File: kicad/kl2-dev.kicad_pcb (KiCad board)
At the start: 2 copper layers, 34.3 x 19 mm, 16 parts, among them CON1 USB-MINI-B, P1 CONN_13, P2 CONN_13, P3 TST, U1 MKL26Z32VFM4, X1 CRYSTAL

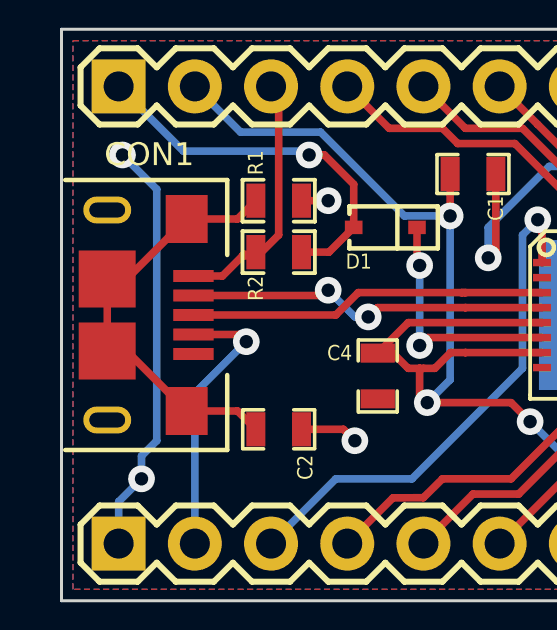
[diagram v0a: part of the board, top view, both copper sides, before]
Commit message: Fixed oval holes to be large circles
OSHPark didn't handle them very well
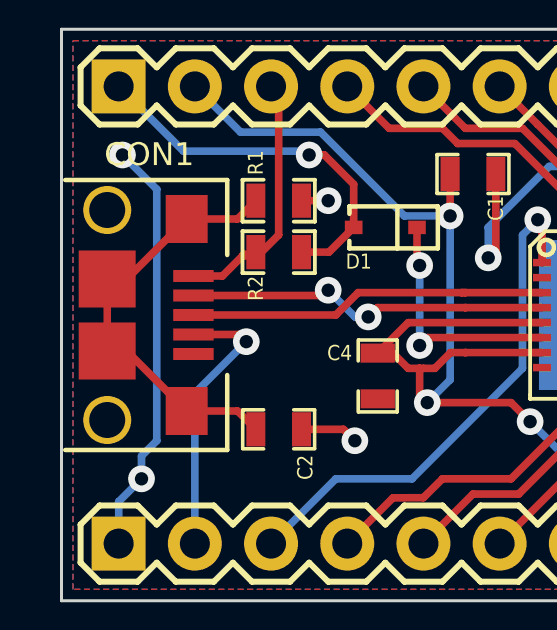
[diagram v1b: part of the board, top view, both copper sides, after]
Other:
- board text added: "kl2-dev"
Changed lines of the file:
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@@
     (links 58)
     (no_connects 1)
-    (area 33.349767 46.7335 69.265001 69.4674)
+    (area 33.349767 47.3726 69.265001 69.4674)
     (thickness 1.6)
-    (drawings 7)
+    (drawings 6)
     (tracks 261)
     (zones 0)
@@
     (mod_text_size 1 1)
     (mod_text_width 0.15)
-    (pad_size 5 5)
-    (pad_drill 0)
+    (pad_size 1.6 1.6)
+    (pad_drill 1.2)
     (pad_to_mask_clearance 0)
     (aux_axis_origin 0 0)
@@
     )
   )
-  (module USB-MICRO-B (layer F.Cu)
-    (at 36.449 58.42 270)
-    (fp_text reference CON1 (at -5.35 -1.4 360) (layer F.SilkS)
-      (effects (font (size 0.762 0.762) (thickness 0.127)))
-    )
-    (fp_text value USB-MINI-B (at 5.4 -1.35 360) (layer F.SilkS) hide
-      (effects (font (size 0.762 0.762) (thickness 0.127)))
-    )
-    (fp_line (start 4.5 1.4) (end 4.5 -4) (layer F.SilkS) (width 0.15))
-    (fp_line (start 4.5 -4) (end 2 -4) (layer F.SilkS) (width 0.15))
-    (fp_line (start -4.5 1.4) (end -4.5 -4) (layer F.SilkS) (width 0.15))
-    (fp_line (start -4.5 -4) (end -2 -4) (layer F.SilkS) (width 0.15))
-    (pad 6 smd rect (at -1.2 0 270) (size 1.9 1.9)
-      (layers F.Cu F.Paste F.Mask)
-      (net 28 N-0000013)
-    )
-    (pad 7 smd rect (at 1.2 0 270) (size 1.9 1.9)
-      (layers F.Cu F.Paste F.Mask)
-      (net 28 N-0000013)
-    )
-    (pad 8 smd rect (at -3.2 -2.65 270) (size 1.6 1.4)
-      (layers F.Cu F.Paste F.Mask)
-      (net 28 N-0000013)
-    )
-    (pad 9 smd rect (at 3.2 -2.65 270) (size 1.6 1.4)
-      (layers F.Cu F.Paste F.Mask)
-      (net 28 N-0000013)
-    )
-    (pad 3 smd rect (at 0 -2.875 270) (size 0.4 1.35)
-      (layers F.Cu F.Paste F.Mask)
-      (net 26 N-0000011)
-    )
-    (pad 4 smd rect (at 0.65 -2.875 270) (size 0.4 1.35)
-      (layers F.Cu F.Paste F.Mask)
-      (net 2 /ID)
-    )
-    (pad 2 smd rect (at -0.65 -2.875 270) (size 0.4 1.35)
-      (layers F.Cu F.Paste F.Mask)
-      (net 27 N-0000012)
-    )
-    (pad 1 smd rect (at -1.3 -2.875 270) (size 0.4 1.35)
-      (layers F.Cu F.Paste F.Mask)
-      (net 31 N-0000025)
-    )
-    (pad 5 smd rect (at 1.3 -2.875 270) (size 0.4 1.35)
-      (layers F.Cu F.Paste F.Mask)
-      (net 25 GND)
-    )
-    (pad 10 thru_hole oval (at -3.5 0 270) (size 0.9 1.6) (drill oval 0.5 1.2)
-      (layers *.Cu *.Mask F.SilkS)
-    )
-    (pad 11 thru_hole oval (at 3.5 0 270) (size 0.9 1.6) (drill oval 0.5 1.2)
-      (layers *.Cu *.Mask F.SilkS)
-    )
-  )
   (module SOD323 (layer F.Cu)
     (at 45.72 55.499)
@@
     )
   )
+  (module USB-MICRO-B (layer F.Cu)
+    (at 36.449 58.42 270)
+    (fp_text reference CON1 (at -5.35 -1.4 360) (layer F.SilkS)
+      (effects (font (size 0.762 0.762) (thickness 0.127)))
+    )
+    (fp_text value USB-MINI-B (at 5.4 -1.35 360) (layer F.SilkS) hide
+      (effects (font (size 0.762 0.762) (thickness 0.127)))
+    )
+    (fp_line (start 4.5 1.4) (end 4.5 -4) (layer F.SilkS) (width 0.15))
+    (fp_line (start 4.5 -4) (end 2 -4) (layer F.SilkS) (width 0.15))
+    (fp_line (start -4.5 1.4) (end -4.5 -4) (layer F.SilkS) (width 0.15))
+    (fp_line (start -4.5 -4) (end -2 -4) (layer F.SilkS) (width 0.15))
+    (pad 6 smd rect (at -1.2 0 270) (size 1.9 1.9)
+      (layers F.Cu F.Paste F.Mask)
+      (net 28 N-0000013)
+    )
+    (pad 7 smd rect (at 1.2 0 270) (size 1.9 1.9)
+      (layers F.Cu F.Paste F.Mask)
+      (net 28 N-0000013)
+    )
+    (pad 8 smd rect (at -3.2 -2.65 270) (size 1.6 1.4)
+      (layers F.Cu F.Paste F.Mask)
+      (net 28 N-0000013)
+    )
+    (pad 9 smd rect (at 3.2 -2.65 270) (size 1.6 1.4)
+      (layers F.Cu F.Paste F.Mask)
+      (net 28 N-0000013)
+    )
+    (pad 3 smd rect (at 0 -2.875 270) (size 0.4 1.35)
+      (layers F.Cu F.Paste F.Mask)
+      (net 26 N-0000011)
+    )
+    (pad 4 smd rect (at 0.65 -2.875 270) (size 0.4 1.35)
+      (layers F.Cu F.Paste F.Mask)
+      (net 2 /ID)
+    )
+    (pad 2 smd rect (at -0.65 -2.875 270) (size 0.4 1.35)
+      (layers F.Cu F.Paste F.Mask)
+      (net 27 N-0000012)
+    )
+    (pad 1 smd rect (at -1.3 -2.875 270) (size 0.4 1.35)
+      (layers F.Cu F.Paste F.Mask)
+      (net 31 N-0000025)
+    )
+    (pad 5 smd rect (at 1.3 -2.875 270) (size 0.4 1.35)
+      (layers F.Cu F.Paste F.Mask)
+      (net 25 GND)
+    )
+    (pad 10 thru_hole circle (at -3.5 0 270) (size 1.6 1.6) (drill 1.2)
+      (layers *.Cu *.Mask F.SilkS)
+    )
+    (pad 11 thru_hole circle (at 3.5 0 270) (size 1.6 1.6) (drill 1.2)
+      (layers *.Cu *.Mask F.SilkS)
+    )
+  )
+  (gr_text kl2-dev (at 39.37 58.42 270) (layer B.SilkS)
+    (effects (font (size 1.5 1.5) (thickness 0.3)) (justify mirror))
+  )
   (gr_line (start 34.925 67.945) (end 34.925 48.895) (angle 90) (layer Edge.Cuts) (width 0.1))
   (gr_line (start 69.215 67.945) (end 34.925 67.945) (angle 90) (layer Edge.Cuts) (width 0.1))
   (gr_line (start 69.215 48.895) (end 69.215 67.945) (angle 90) (layer Edge.Cuts) (width 0.1))
   (gr_line (start 34.925 48.895) (end 69.215 48.895) (angle 90) (layer Edge.Cuts) (width 0.1))
-  (target plus (at 39.624 46.736) (size 0.005) (width 0.1) (layer Edge.Cuts))
-  (target plus (at 39.624 46.736) (size 0.005) (width 0.1) (layer Edge.Cuts))
   (target plus (at 36.83 50.8) (size 0.005) (width 0.1) (layer Edge.Cuts))
   (segment (start 47.117 61.341) (end 49.911 61.341) (width 0.254) (layer F.Cu) (net 1))

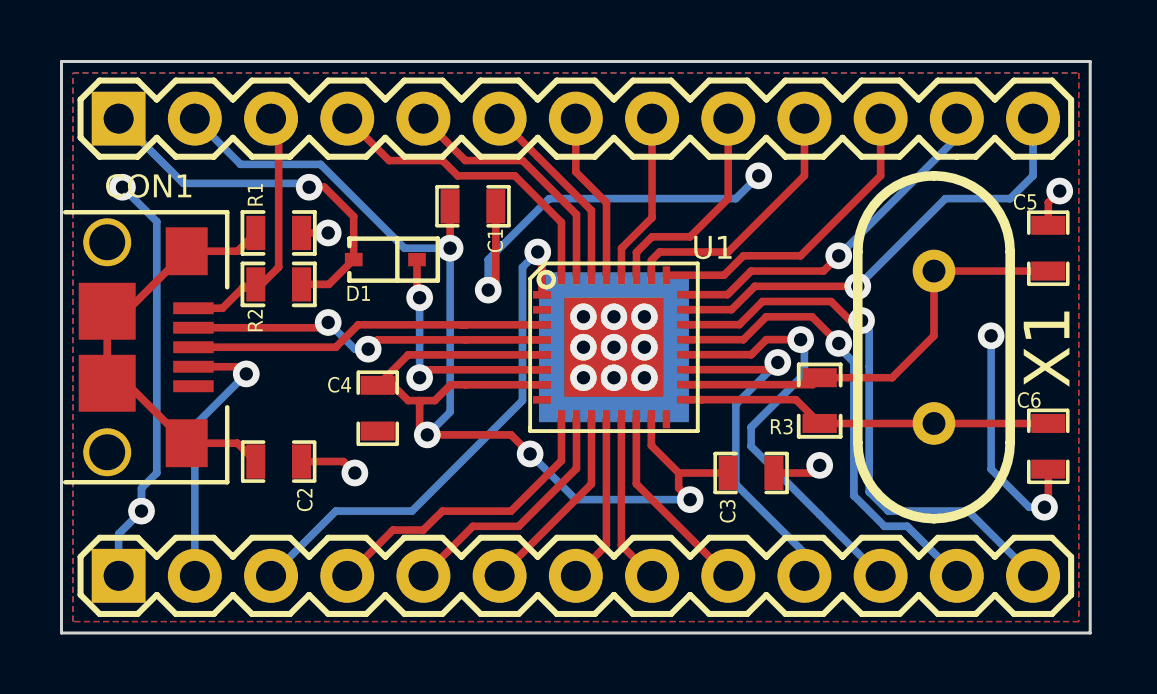
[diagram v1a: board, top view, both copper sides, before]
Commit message: Reduced thermal via size to minimum drill diameter
TI has a paper about this and said to keep the via size <0.3mm (we can't quite
get that small, but we can get close) and to have the spacing of thermal vias
be about 1mm (we had this already by happenstance)
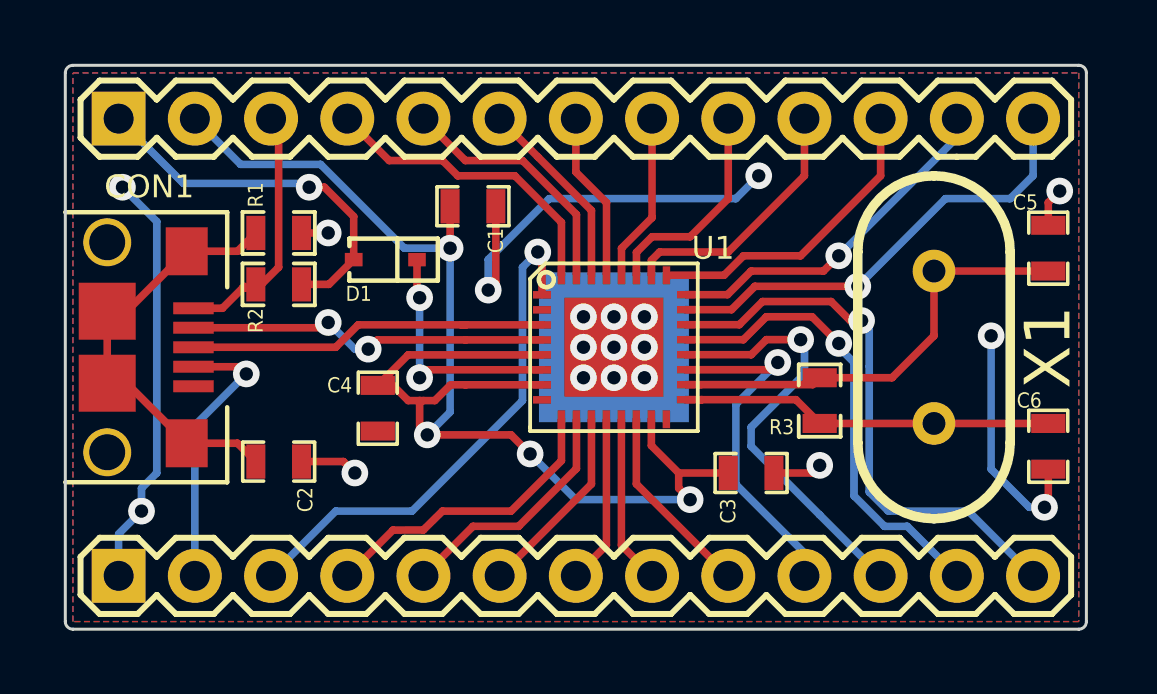
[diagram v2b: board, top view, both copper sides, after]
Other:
- board size 34.3 x 19 mm -> 34 x 18.8 mm
- net class Thermal added: clearance 0.1524, trace_width 0.254, via_dia 0.5588, via_drill 0.3302
- rule via_min_drill: 0.508 -> 0.3302
- rule via_min_size: 0.889 -> 0.508
- board text added: "KL2x ARM Dev Board Kevin Cuzner"
- board text removed: "kl2-dev"
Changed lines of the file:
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@@
     (links 58)
     (no_connects 1)
-    (area 33.349767 47.3726 69.265001 69.4674)
+    (area 33.270372 47.3726 69.138001 69.4674)
     (thickness 1.6)
-    (drawings 6)
+    (drawings 10)
     (tracks 261)
     (zones 0)
@@
     (via_size 0.889)
     (via_drill 0.635)
-    (via_min_size 0.889)
-    (via_min_drill 0.508)
+    (via_min_size 0.508)
+    (via_min_drill 0.3302)
     (uvia_size 0.508)
     (uvia_drill 0.127)
@@
     (add_net /PTE0)
     (add_net /PTE30)
-    (add_net /U1_THERM)
     (add_net GND)
     (add_net N-0000011)
@@
     (add_net N-000003)
     (add_net VDD)
+  )
+  (net_class Thermal ""
+    (clearance 0.1524)
+    (trace_width 0.254)
+    (via_dia 0.5588)
+    (via_drill 0.3302)
+    (uvia_dia 0.508)
+    (uvia_drill 0.127)
+    (add_net /U1_THERM)
   )
   (module SM0603_Resistor (layer F.Cu)
@@
     )
   )
-  (gr_text kl2-dev (at 39.37 58.42 270) (layer B.SilkS)
-    (effects (font (size 1.5 1.5) (thickness 0.3)) (justify mirror))
-  )
-  (gr_line (start 34.925 67.945) (end 34.925 48.895) (angle 90) (layer Edge.Cuts) (width 0.1))
-  (gr_line (start 69.215 67.945) (end 34.925 67.945) (angle 90) (layer Edge.Cuts) (width 0.1))
-  (gr_line (start 69.215 48.895) (end 69.215 67.945) (angle 90) (layer Edge.Cuts) (width 0.1))
-  (gr_line (start 34.925 48.895) (end 69.215 48.895) (angle 90) (layer Edge.Cuts) (width 0.1))
+  (gr_line (start 68.834 67.818) (end 35.306 67.818) (angle 90) (layer Edge.Cuts) (width 0.1))
+  (gr_line (start 69.088 49.276) (end 69.088 67.564) (angle 90) (layer Edge.Cuts) (width 0.1))
+  (gr_line (start 35.306 49.022) (end 68.834 49.022) (angle 90) (layer Edge.Cuts) (width 0.1))
+  (gr_line (start 35.052 67.564) (end 35.052 49.276) (angle 90) (layer Edge.Cuts) (width 0.1))
+  (gr_arc (start 35.306 67.564) (end 35.306 67.818) (angle 90) (layer Edge.Cuts) (width 0.1))
+  (gr_arc (start 68.834 67.564) (end 69.088 67.564) (angle 90) (layer Edge.Cuts) (width 0.1))
+  (gr_arc (start 68.834 49.276) (end 68.834 49.022) (angle 90) (layer Edge.Cuts) (width 0.1))
+  (gr_arc (start 35.306 49.276) (end 35.052 49.276) (angle 90) (layer Edge.Cuts) (width 0.1))
+  (gr_text "KL2x ARM Dev Board\nKevin Cuzner" (at 39.37 58.42 90) (layer B.SilkS)
+    (effects (font (size 0.762 0.762) (thickness 0.1524)) (justify mirror))
+  )
   (target plus (at 36.83 50.8) (size 0.005) (width 0.1) (layer Edge.Cuts))
   (segment (start 47.117 61.341) (end 49.911 61.341) (width 0.254) (layer F.Cu) (net 1))

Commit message: Added usb resistors and fixed diode packaging
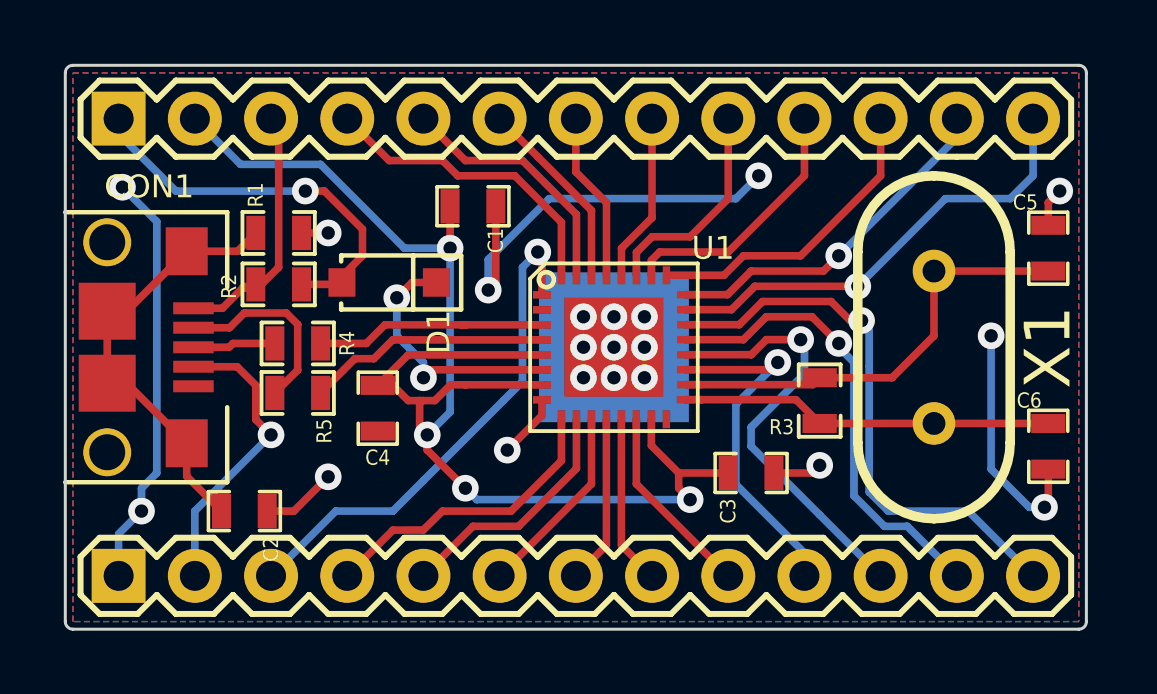
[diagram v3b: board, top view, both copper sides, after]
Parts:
- added R4: 33, SM0603_Resistor, F.Cu at (42.8, 58.3)
- added R5: 33, SM0603_Resistor, F.Cu at (42.8, 59.9)
- C2: value 4.7n -> 4700p
- D1: footprint SOD323 -> SOD123
- moved C2 2.01 mm to (41.0, 63.9)
- moved D1 0.77 mm to (45.8, 56.3)
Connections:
- CON1 pad 2: N-0000012 -> N-0000013
- U1 pad 3: N-0000011 -> N-0000010
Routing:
- net N-0000011: track 12.1 -> 2.77 mm
- net N-0000010: track 0.00 -> 7.78 mm
- net N-0000013: track 0.00 -> 6.44 mm
- net N-0000012: track 12.2 -> 8.11 mm, vias 2 -> 0
- net GND: track 41.9 -> 44.6 mm, vias 10 -> 11
- net VDD: track 12.7 -> 13.4 mm
- net /ID: track 9.30 -> 9.95 mm

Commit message: Final schematic and pcb sent to fabricator
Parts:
- moved C2 1.55 mm to (42.5, 63.6)
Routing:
- net N-000006: track 14.7 -> 15.7 mm
- net GND: track 44.6 -> 43.9 mm
